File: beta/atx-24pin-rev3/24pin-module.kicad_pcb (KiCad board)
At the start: 4 copper layers, 73 parts, among them J1 TO-HUB, J2 TO-HUB-PWR, J3 ATX-24 PSU, J5 USB-C 2.0, J6 TO-HUB-STACK, SW1 BOOT, SW2 RESET, U1 ESP32-C6-MINI-1-N4, U10 INA238, U11 INA238, U12 INA238, U13 INA238, U2 TJA1051T/3, U3 LP5907MFX-3.3, U5 TPS2121RUXR, U612V1 INA181A2IDBVR, U65V1 INA181A2IDBVR, U712V1 TLV7011DBVR, U75V1 TLV7011DBVR

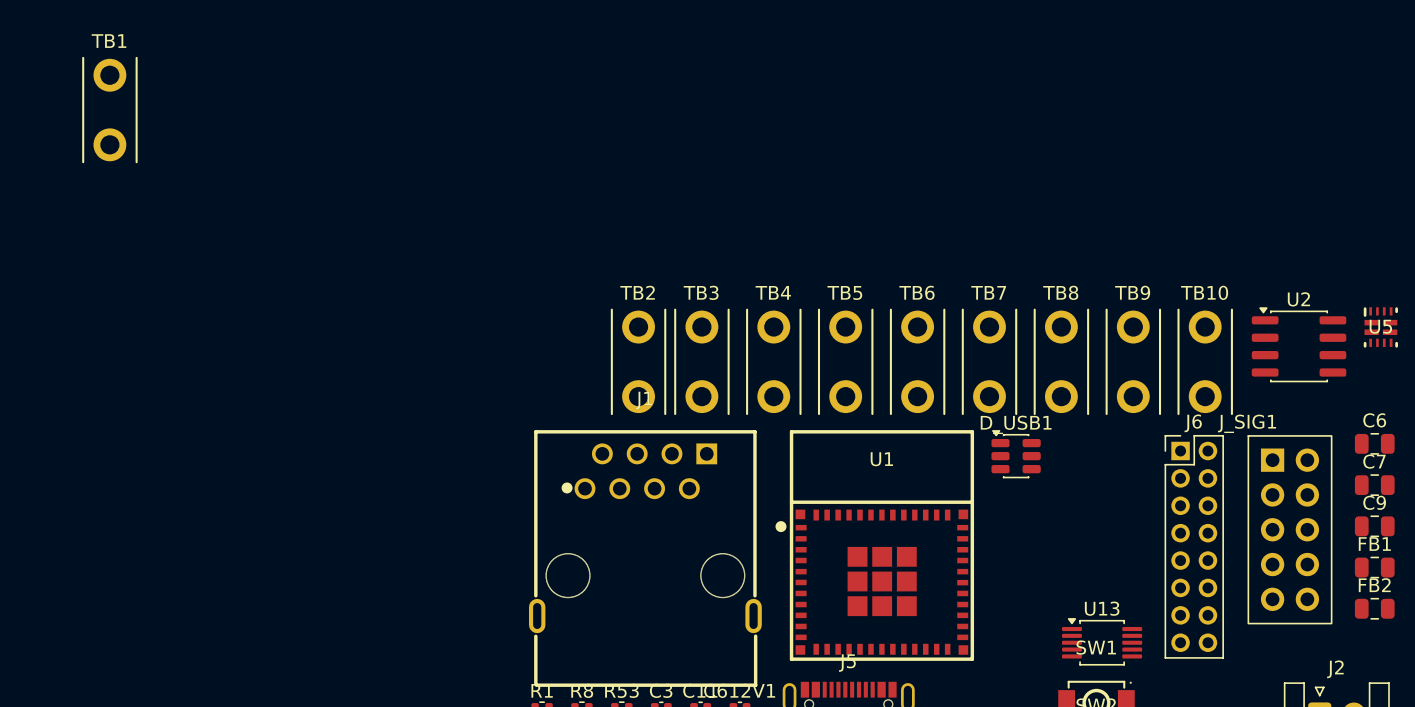
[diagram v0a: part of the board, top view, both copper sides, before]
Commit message: pipeline: integrate route-aware physical design flow
Generalize critical-first placement and routing, future-congestion and power-authority planning, route provenance, process watchdogs, fab/thermal validation, dashboard review, and XFCN integration. Add the supporting board contracts, component libraries, documentation, and regression coverage.
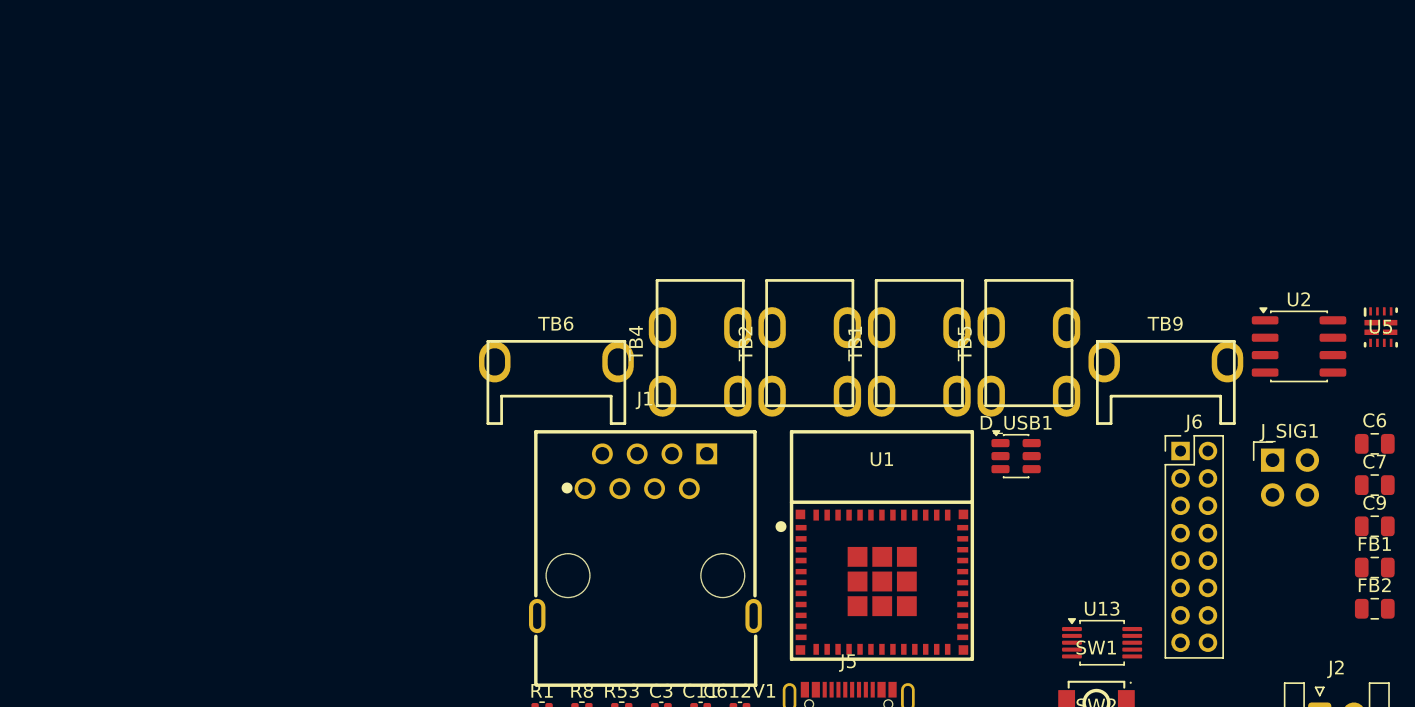
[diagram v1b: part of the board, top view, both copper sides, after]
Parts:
- removed TB10, TB3, TB7, TB8: TE 63969-1, cec-Connector_Blade:TE_63969_FASTON_Receptacle_250_Vertical_THT
- J_SIG1: value CEC_CONN_2x5 -> SSQ-102-03-G-D; footprint cec-Connector_PinHeader_2.54mm:PinHeader_2x05_P2.54mm_Vertical -> cec-Connector_PinSocket_2.54mm:Samtec_SSQ-102-03-G-D_2x02_P2.54mm_Vertical
- TB1, TB2, TB4, TB5: value TE 63969-1 -> XFCN T34069; footprint cec-Connector_Blade:TE_63969_FASTON_Receptacle_250_Vertical_THT -> cec-Connector_Screw:XFCN_T34069_THT_M3_40A
- TB6, TB9: value TE 63969-1 -> TTR32100127-0600; footprint cec-Connector_Blade:TE_63969_FASTON_Receptacle_250_Vertical_THT -> cec-Connector_Screw:XFCN_TTR32100127-0600_THT_M3_60A
- moved TB1 61.9 mm to (216.5, 74.4), turned to 90 degrees
- moved TB6 26.4 mm to (190.0, 74.4)
- moved TB5 13.4 mm to (224.5, 74.4), turned to 90 degrees
- moved TB2 12.5 mm to (208.5, 74.4), turned to 90 degrees
- moved TB4 5.38 mm to (200.5, 74.4), turned to 90 degrees
- moved TB9 2.38 mm to (234.5, 74.4)
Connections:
- J_SIG1 pad 1: /ATX_PSON -> /ATX INTERPOSER + CONTROL SIGNALS/ATX_NEG12V
- J_SIG1 pad 2: /ATX_PWROK -> /ATX INTERPOSER + CONTROL SIGNALS/ATX_PSON
- J_SIG1 pad 3: /ATX_NEG12V -> /ATX INTERPOSER + CONTROL SIGNALS/ATX_PWROK
